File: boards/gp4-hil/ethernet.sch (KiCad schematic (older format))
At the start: 32 parts, among them J1 BEL_FUSE_0826-1G1T-23-F, U2 XC7A100T-1FTG256C, U5 KSZ9031RN

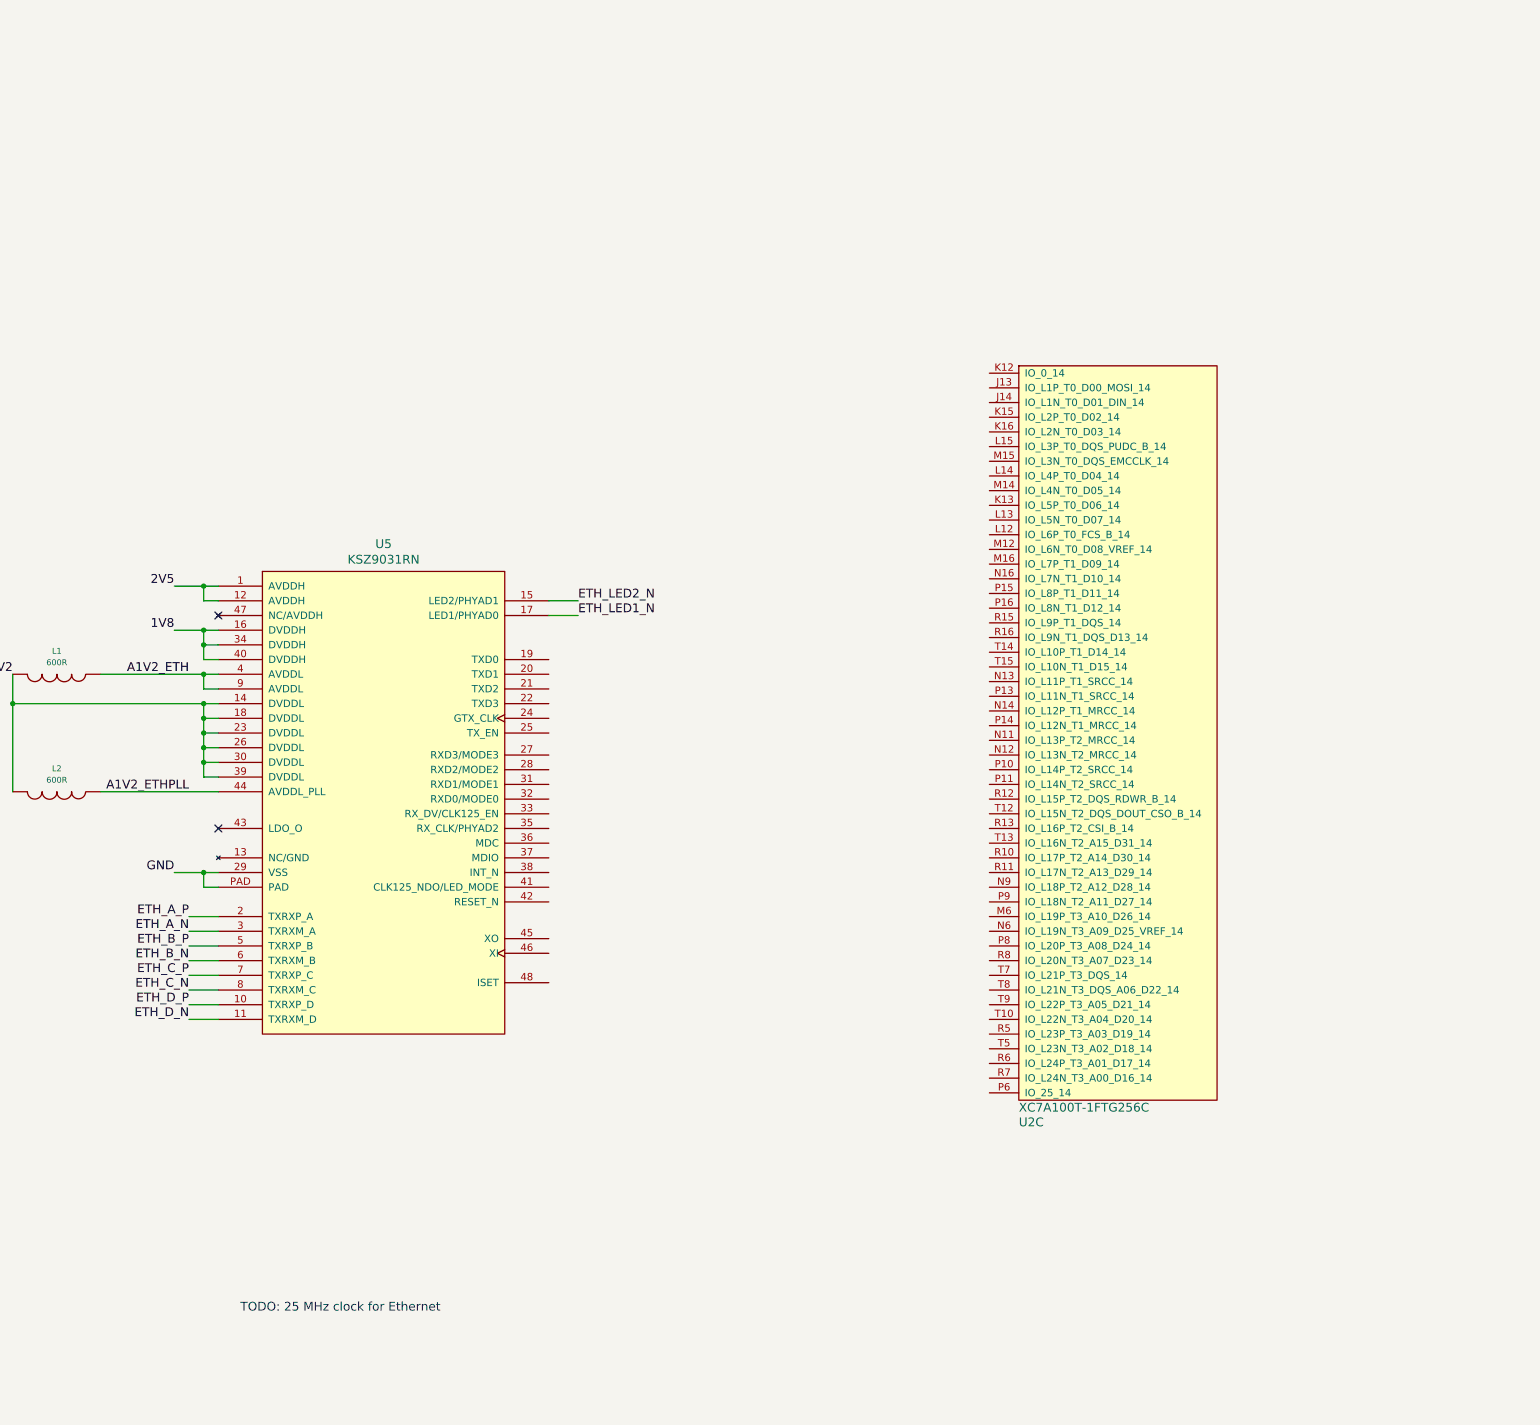
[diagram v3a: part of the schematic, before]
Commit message: Continued analog input schematic
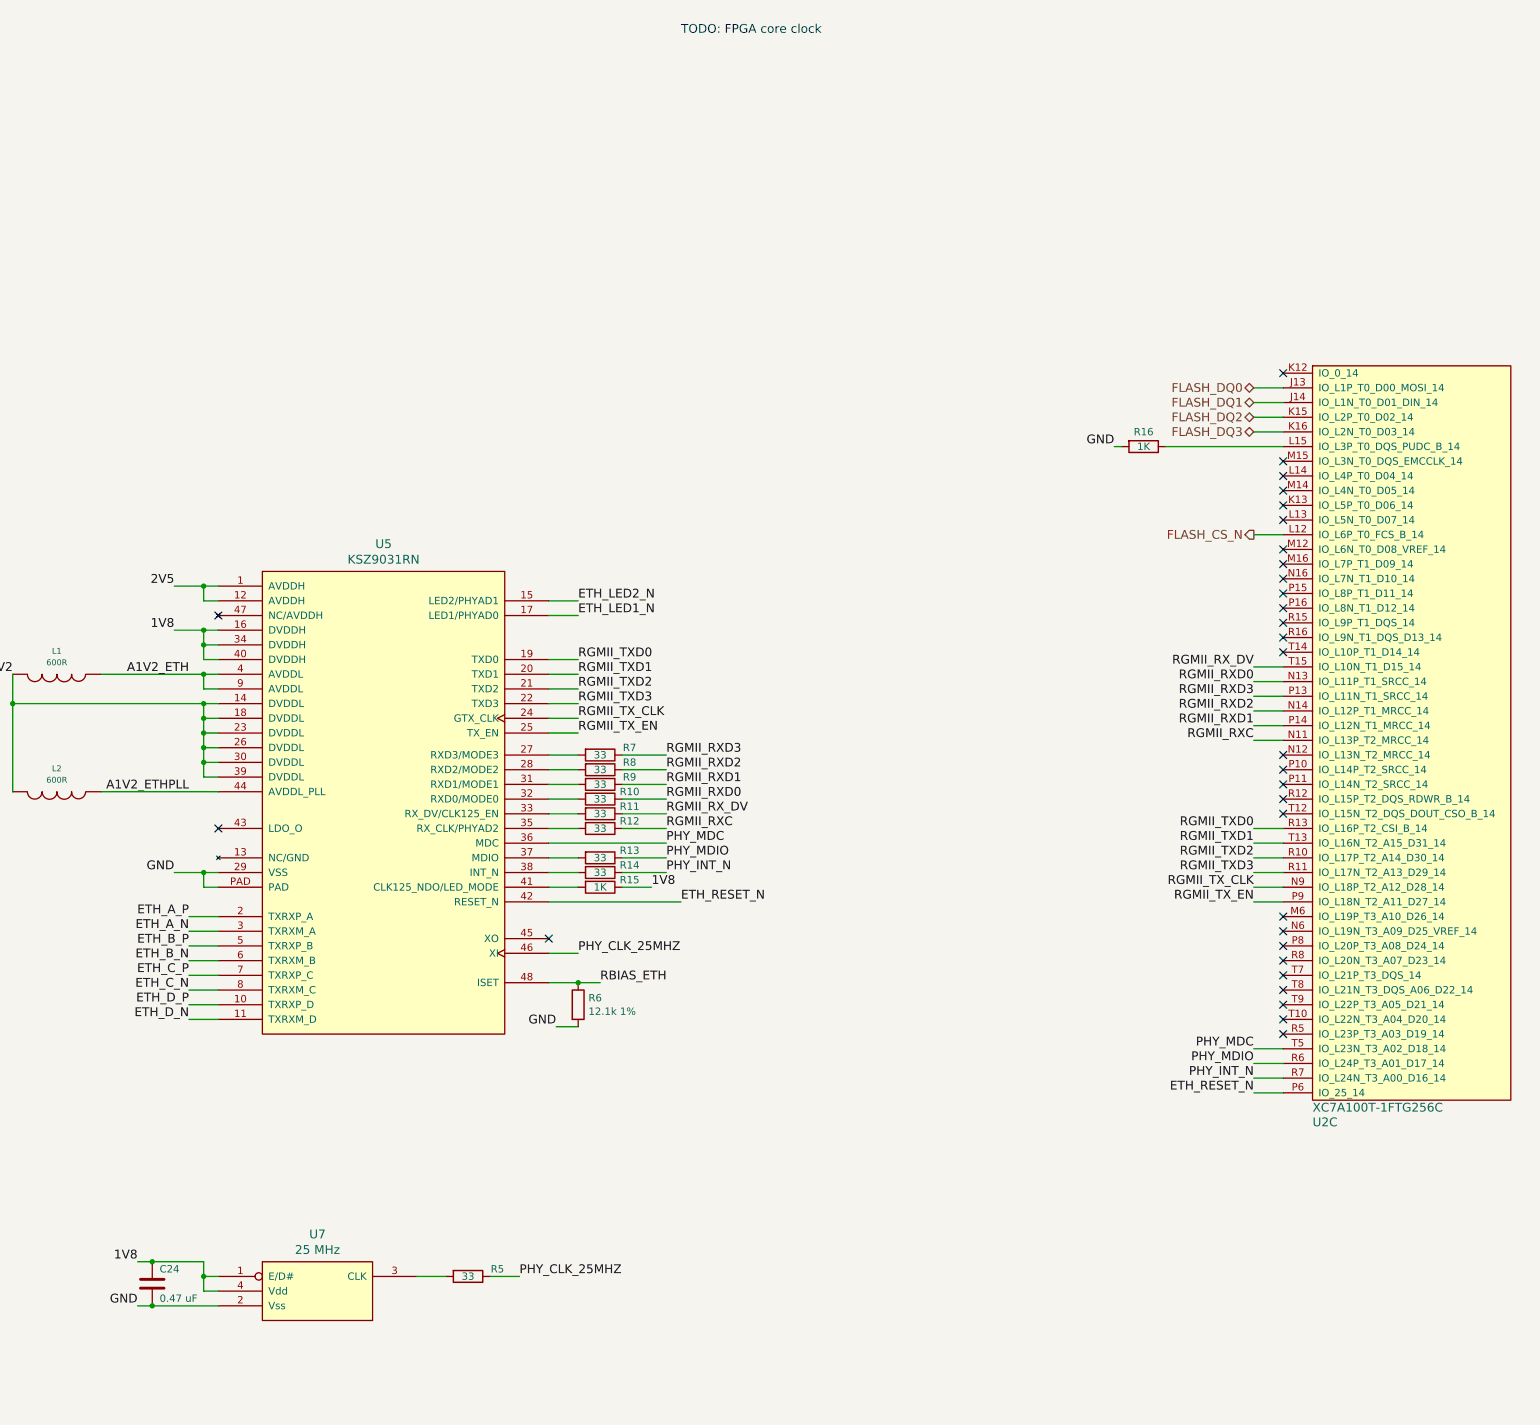
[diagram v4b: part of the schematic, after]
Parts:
- added C24: 0.47 uF, symbol C
- added R10, R11, R12, R13, R14, R5, R7, R8, R9: 33, symbol R
- added R15, R16: 1K, symbol R
- added R6: 12.1k 1%, symbol R
- added U7: 25 MHz, symbol OSC
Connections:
- net 1V8: now also C24.1, R15.1, U7.1 (E/D#), U7.4 (Vdd)
- net GND: now also C24.2, R16.2, R6.2, U7.2 (Vss)
- net RGMII_TXD0: now reaches U5.19 (TXD0)
- net RGMII_TXD0: now also U2.R13 (IO_L16P_T2_CSI_B_14)
- net RGMII_TXD1: now reaches U5.20 (TXD1)
- net RGMII_TXD1: now also U2.T13 (IO_L16N_T2_A15_D31_14)
- net RGMII_TXD2: now reaches U5.21 (TXD2)
- net RGMII_TXD2: now also U2.R10 (IO_L17P_T2_A14_D30_14)
- net RGMII_TXD3: now reaches U5.22 (TXD3)
- net RGMII_TXD3: now also U2.R11 (IO_L17N_T2_A13_D29_14)
- net RGMII_TX_CLK: now reaches U5.24 (GTX_CLK)
- net RGMII_TX_CLK: now also U2.N9 (IO_L18P_T2_A12_D28_14)
- net RGMII_TX_EN: now reaches U5.25 (TX_EN)
- net RGMII_TX_EN: now also U2.P9 (IO_L18N_T2_A11_D27_14)
- net at U5.27 (RXD3/MODE3): now also R7.2
- net at U5.28 (RXD2/MODE2): now also R8.2
- net at U5.31 (RXD1/MODE1): now also R9.2
- net at U5.32 (RXD0/MODE0): now also R10.2
- net at U5.33 (RX_DV/CLK125_EN): now also R11.2
- net at U5.35 (RX_CLK/PHYAD2): now also R12.2
- net PHY_MDC: now reaches U5.36 (MDC)
- net PHY_MDC: now also U2.T5 (IO_L23N_T3_A02_D18_14)
- net at U5.37 (MDIO): now also R13.2
- net at U5.38 (INT_N): now also R14.2
- net at U5.41 (CLK125_NDO/LED_MODE): now also R15.2
- net ETH_RESET_N: now reaches U5.42 (RESET_N)
- net ETH_RESET_N: now also U2.P6 (IO_25_14)
- net PHY_CLK_25MHZ: now reaches U5.46 (XI)
- net PHY_CLK_25MHZ: now also R5.1
- net RBIAS_ETH: now reaches U5.48 (ISET)
- net RBIAS_ETH: now also R6.1
- net FLASH_DQ0: now reaches U2.J13 (IO_L1P_T0_D00_MOSI_14)
- net FLASH_DQ1: now reaches U2.J14 (IO_L1N_T0_D01_DIN_14)
- net FLASH_DQ2: now reaches U2.K15 (IO_L2P_T0_D02_14)
- net FLASH_DQ3: now reaches U2.K16 (IO_L2N_T0_D03_14)
- net FLASH_CS_N: now reaches U2.L12 (IO_L6P_T0_FCS_B_14)
- net at U2.L15 (IO_L3P_T0_DQS_PUDC_B_14): now also R16.1
- net RGMII_RXC: now reaches U2.N11 (IO_L13P_T2_MRCC_14)
- net RGMII_RXC: now also R12.1
- net RGMII_RXD0: now reaches U2.N13 (IO_L11P_T1_SRCC_14)
- net RGMII_RXD0: now also R10.1
- net RGMII_RXD2: now reaches U2.N14 (IO_L12P_T1_MRCC_14)
- net RGMII_RXD2: now also R8.1
- net RGMII_RXD3: now reaches U2.P13 (IO_L11N_T1_SRCC_14)
- net RGMII_RXD3: now also R7.1
- net RGMII_RXD1: now reaches U2.P14 (IO_L12N_T1_MRCC_14)
- net RGMII_RXD1: now also R9.1
- net PHY_MDIO: now reaches U2.R6 (IO_L24P_T3_A01_D17_14)
- net PHY_MDIO: now also R13.1
- net PHY_INT_N: now reaches U2.R7 (IO_L24N_T3_A00_D16_14)
- net PHY_INT_N: now also R14.1
- net RGMII_RX_DV: now reaches U2.T15 (IO_L10N_T1_D15_14)
- net RGMII_RX_DV: now also R11.1
- new net: R5.2, U7.3 (CLK)
- no-connect marks 2 -> 31
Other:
- note added: "TODO: FPGA core clock"
- note removed: "TODO: 25 MHz clock for Ethernet"
- moved on the sheet: U2C

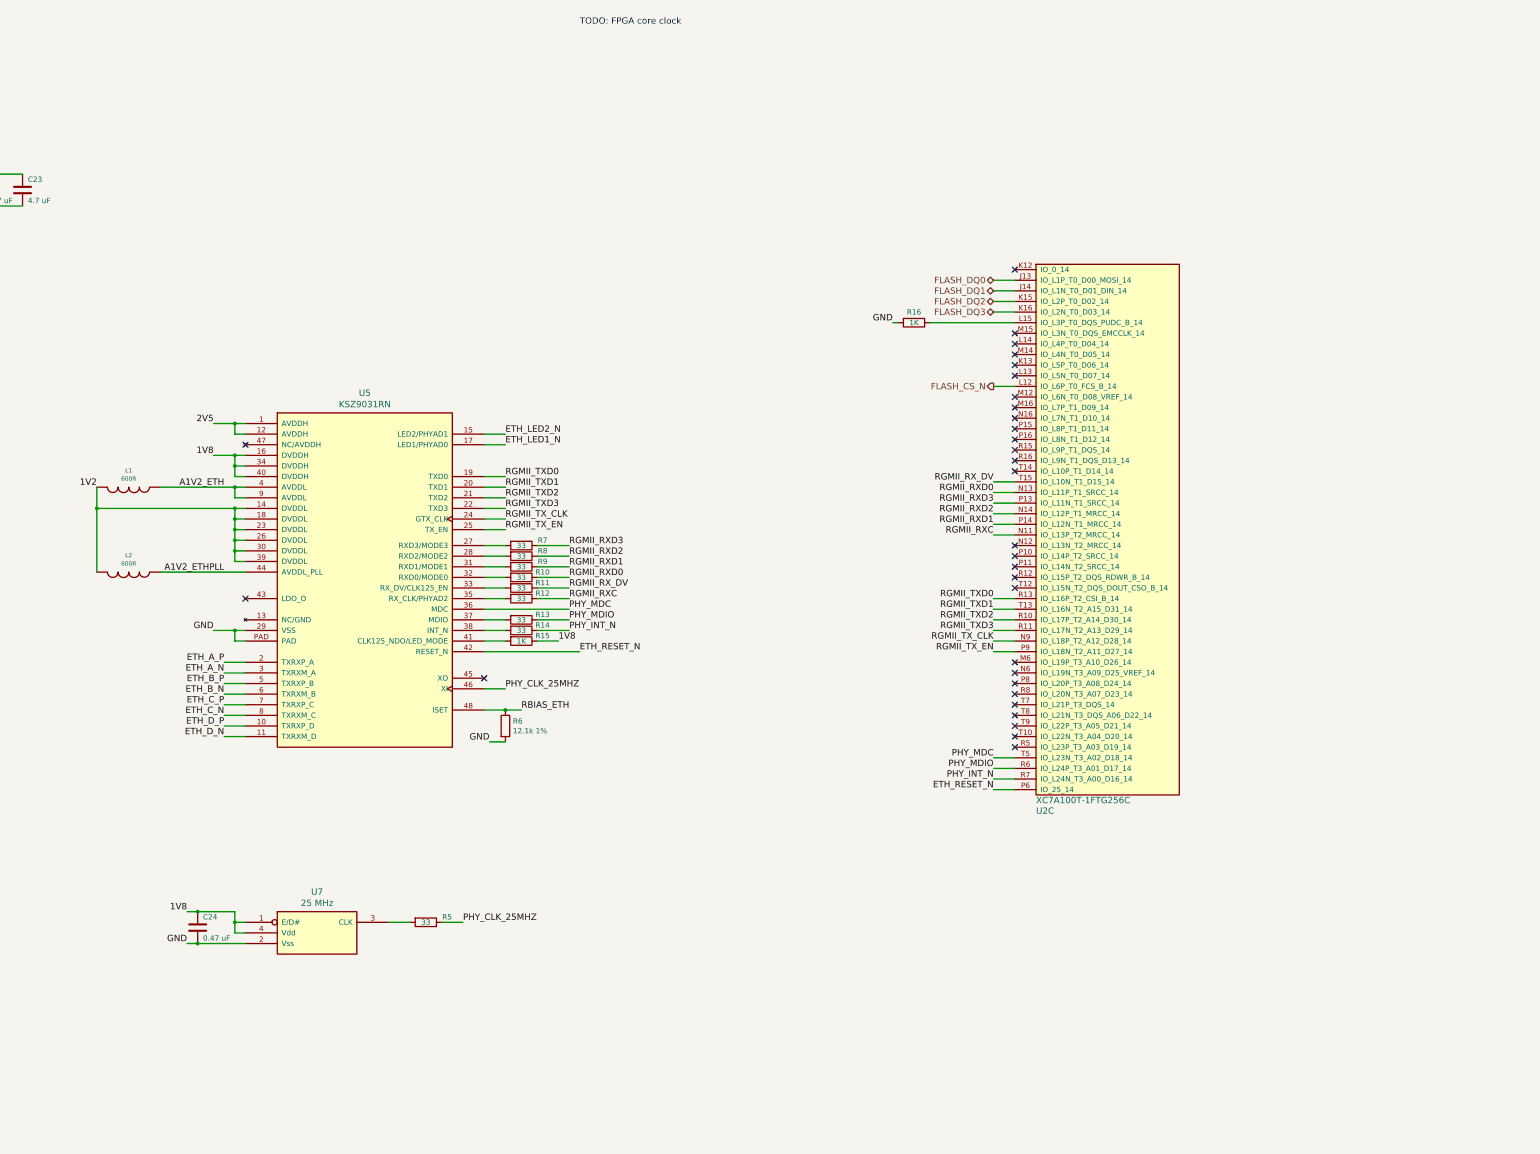
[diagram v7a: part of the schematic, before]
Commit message: Schematic entry for 1V0 PSU
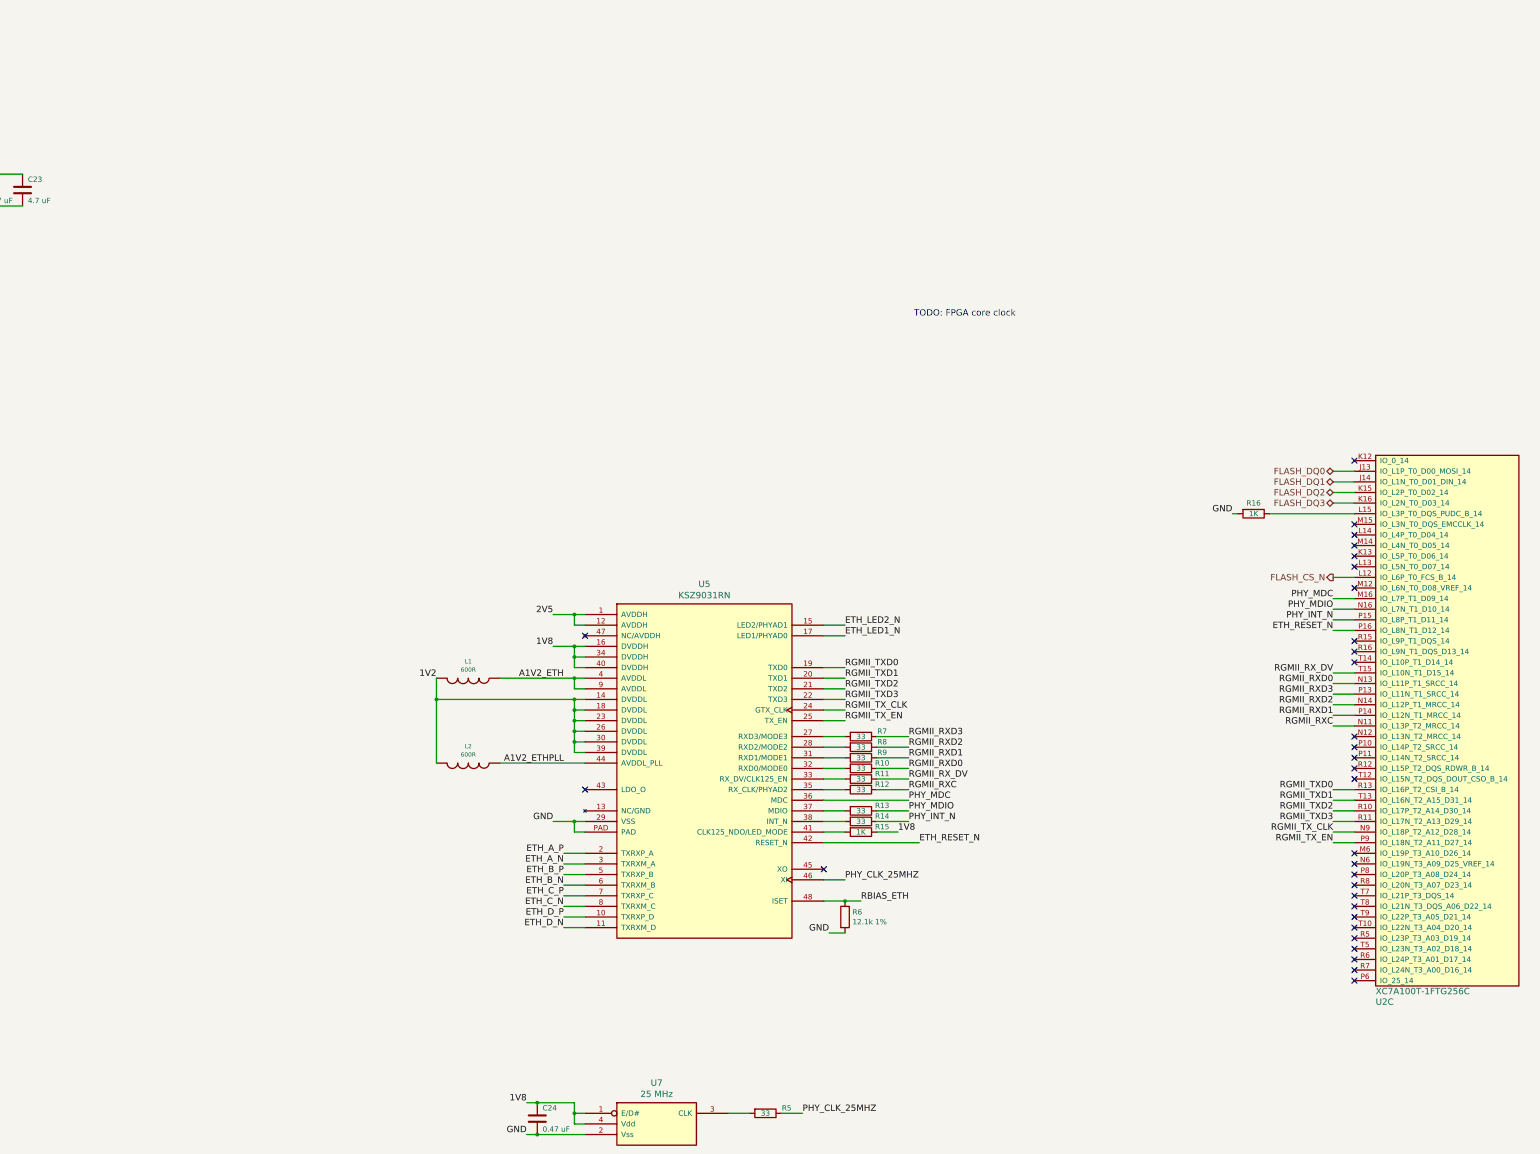
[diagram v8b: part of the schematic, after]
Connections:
- net ETH_RESET_N: now also U2.P16 (IO_L8N_T1_D12_14); no longer U2.P6 (IO_25_14)
- net PHY_INT_N: now also U2.P15 (IO_L8P_T1_D11_14); no longer U2.R7 (IO_L24N_T3_A00_D16_14)
- net PHY_MDC: now also U2.M16 (IO_L7P_T1_D09_14); no longer U2.T5 (IO_L23N_T3_A02_D18_14)
- net PHY_MDIO: now also U2.N16 (IO_L7N_T1_D10_14); no longer U2.R6 (IO_L24P_T3_A01_D17_14)
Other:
- moved on the sheet: C24, L1, L2, R10, R11, R12, R13, R14, R15, R16, R5, R6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
